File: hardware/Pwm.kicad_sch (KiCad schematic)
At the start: 69 parts, among them J10 Conn_01x03_Male, J11 Conn_01x03_Male, J12 Conn_01x03_Male, J13 Conn_01x03_Male, J14 Conn_01x03_Male, J15 Conn_01x03_Male, J16 JST XH, J17 KF350, J18 JST XH, J19 JST XH, J20 KF350, J21 JST XH, J4 JST XH, J5 KF129, J6 KF350, J7 Conn_01x03_Male, J8 Conn_01x03_Male, J9 Conn_01x03_Male, U6 74HCT04

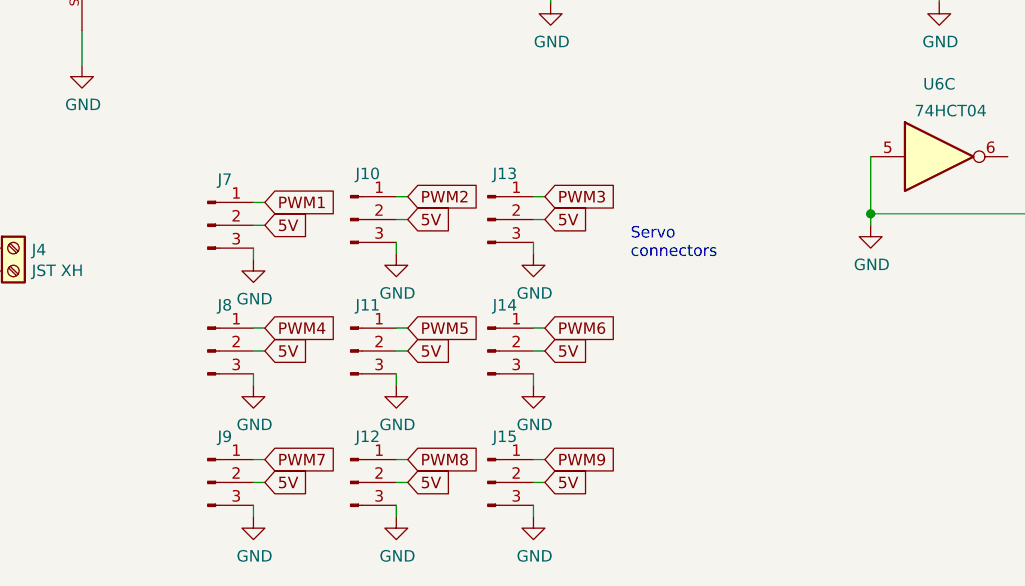
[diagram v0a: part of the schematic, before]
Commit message: Add more input protection. 480 ohm resistors on all direct IO pins. Clamping diodes on the endstops.
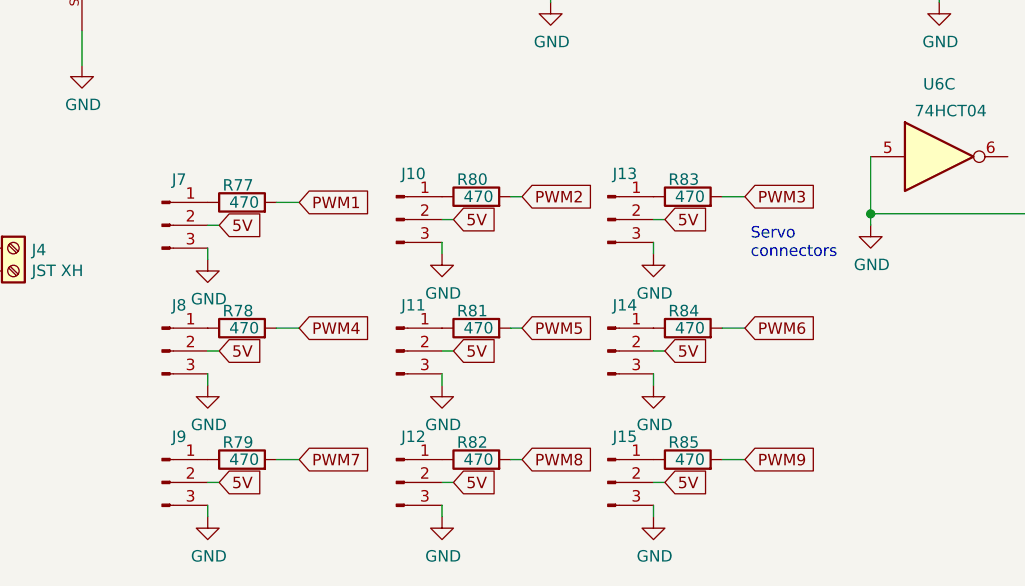
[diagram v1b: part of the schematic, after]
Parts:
- added R77, R78, R79, R80, R81, R82, R83, R84, R85: 470, PrntrBoardV2:R_0603_1608Metric, symbol Device:R
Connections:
- net PWM1: now also R77.2; no longer J7.1 (Pin_1)
- net PWM2: now also R80.2; no longer J10.1 (Pin_1)
- net PWM3: now also R83.2; no longer J13.1 (Pin_1)
- net PWM4: now also R78.2; no longer J8.1 (Pin_1)
- net PWM5: now also R81.2; no longer J11.1 (Pin_1)
- net PWM6: now also R84.2; no longer J14.1 (Pin_1)
- net PWM7: now also R79.2; no longer J9.1 (Pin_1)
- net PWM8: now also R82.2; no longer J12.1 (Pin_1)
- net PWM9: now also R85.2; no longer J15.1 (Pin_1)
- new net: J7.1 (Pin_1), R77.1
- new net: J10.1 (Pin_1), R80.1
- new net: J13.1 (Pin_1), R83.1
- new net: J8.1 (Pin_1), R78.1
- new net: J11.1 (Pin_1), R81.1
- new net: J14.1 (Pin_1), R84.1
- new net: J9.1 (Pin_1), R79.1
- new net: J12.1 (Pin_1), R82.1
- new net: J15.1 (Pin_1), R85.1
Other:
- moved on the sheet: J10, J11, J12, J13, J14, J15, J7, J8, J9

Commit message: Revert "Add more input protection. 480 ohm resistors on all direct IO pins."
This reverts commit 49fdbd5165b8c1709549cdf3235e4b40c9a44330.
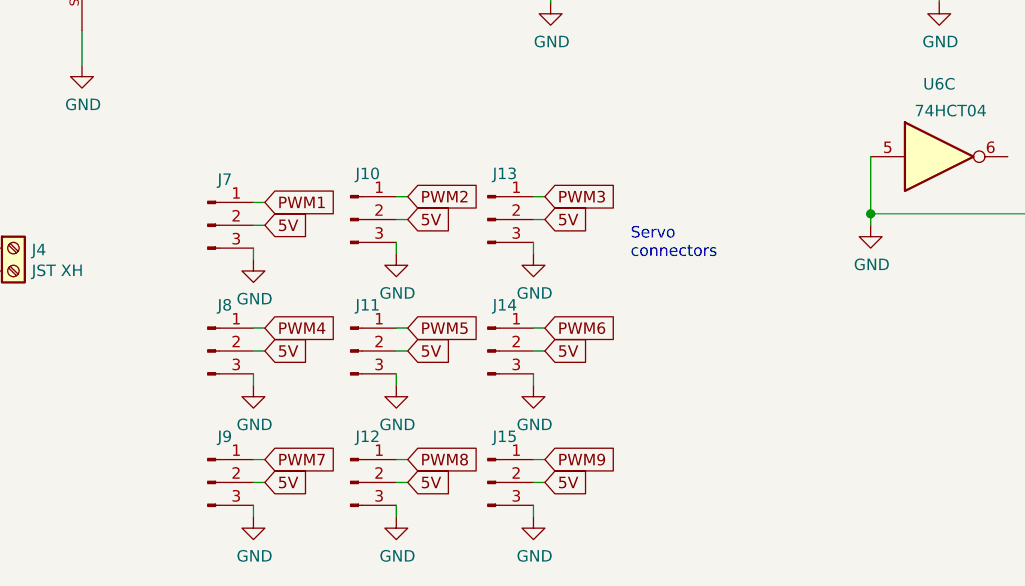
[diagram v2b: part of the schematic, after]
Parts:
- removed R77, R78, R79, R80, R81, R82, R83, R84, R85: 470, PrntrBoardV2:R_0603_1608Metric, symbol Device:R
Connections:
- net PWM1: now also J7.1 (Pin_1)
- net PWM2: now also J10.1 (Pin_1)
- net PWM3: now also J13.1 (Pin_1)
- net PWM4: now also J8.1 (Pin_1)
- net PWM5: now also J11.1 (Pin_1)
- net PWM6: now also J14.1 (Pin_1)
- net PWM7: now also J9.1 (Pin_1)
- net PWM8: now also J12.1 (Pin_1)
- net PWM9: now also J15.1 (Pin_1)
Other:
- moved on the sheet: J10, J11, J12, J13, J14, J15, J7, J8, J9
